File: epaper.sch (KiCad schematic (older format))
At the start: 34 parts, among them Q1 Q_NMOS_GSD, U1 SC18IS602B, U2 e-paper

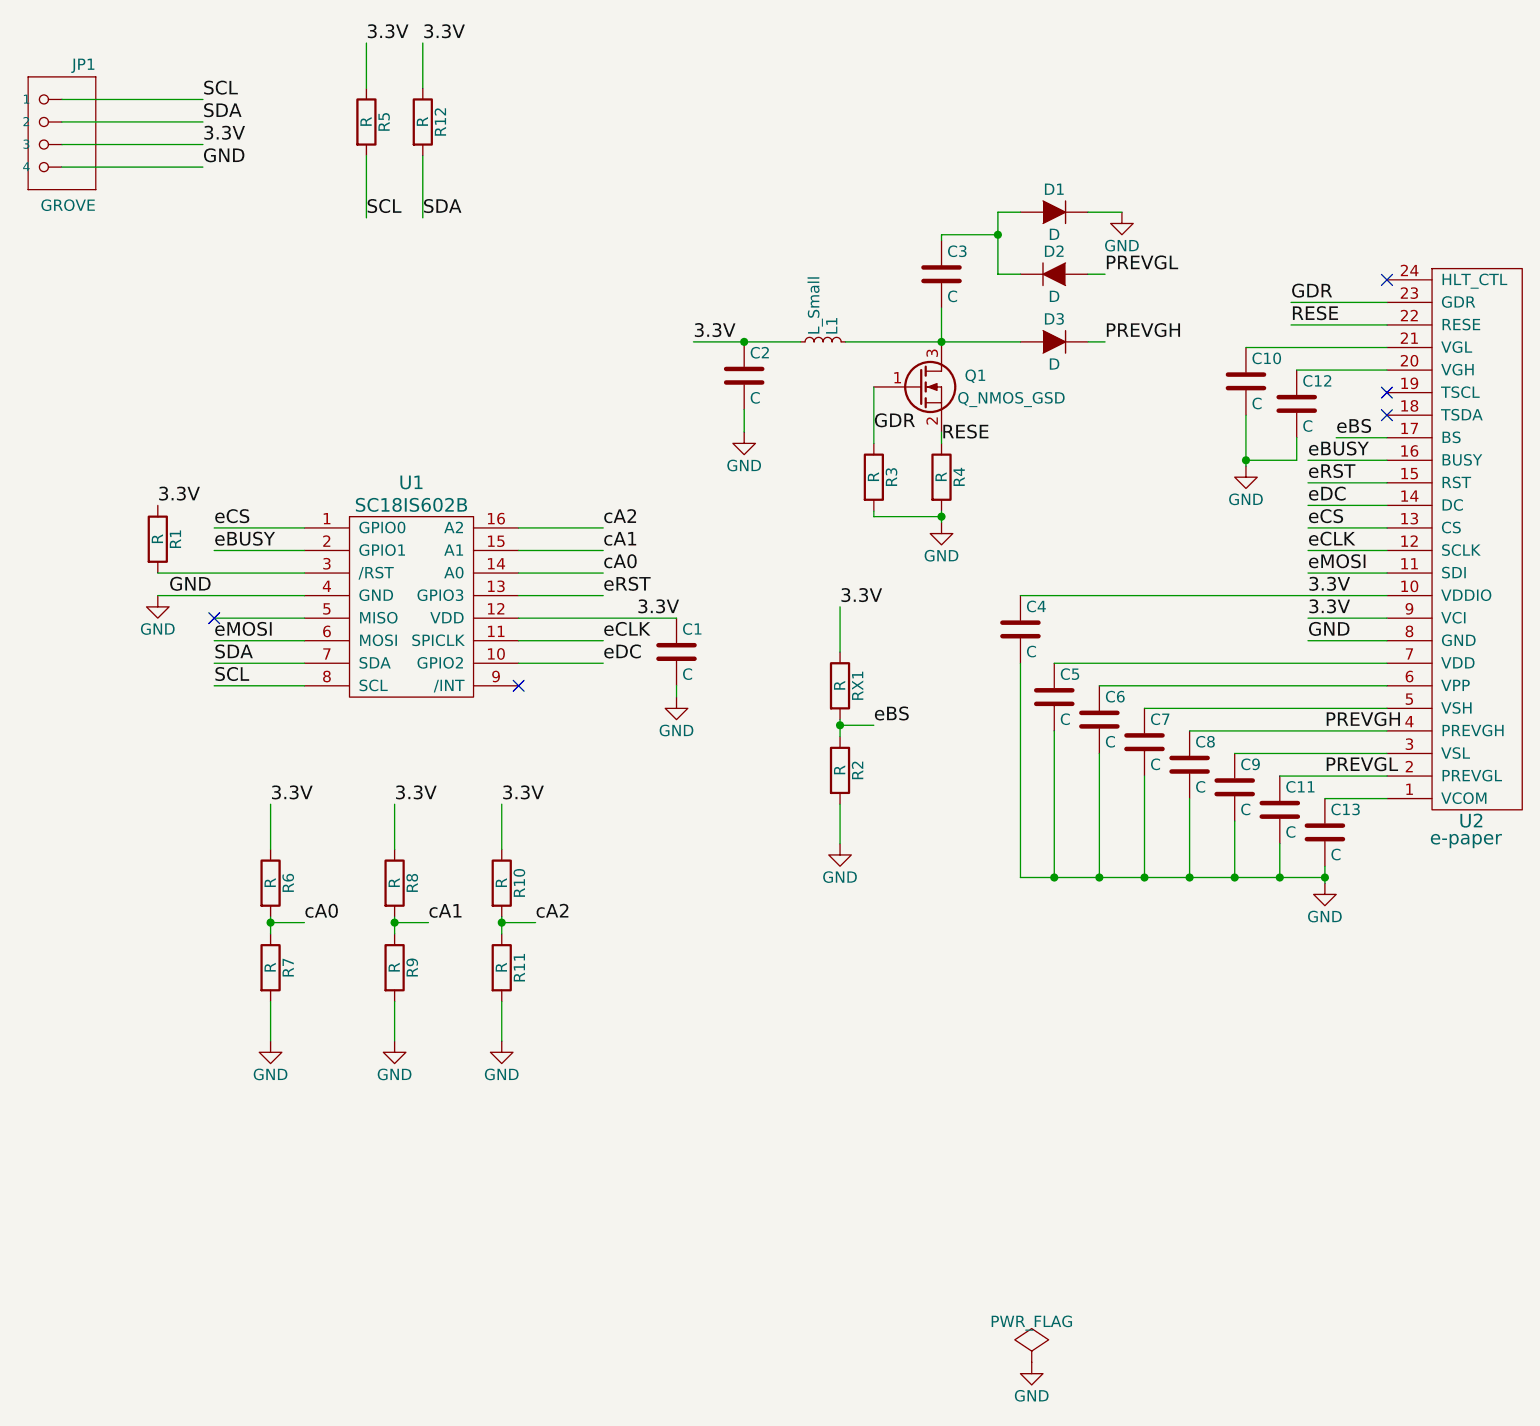
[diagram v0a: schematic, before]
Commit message: Fix the position of the HFL Connector
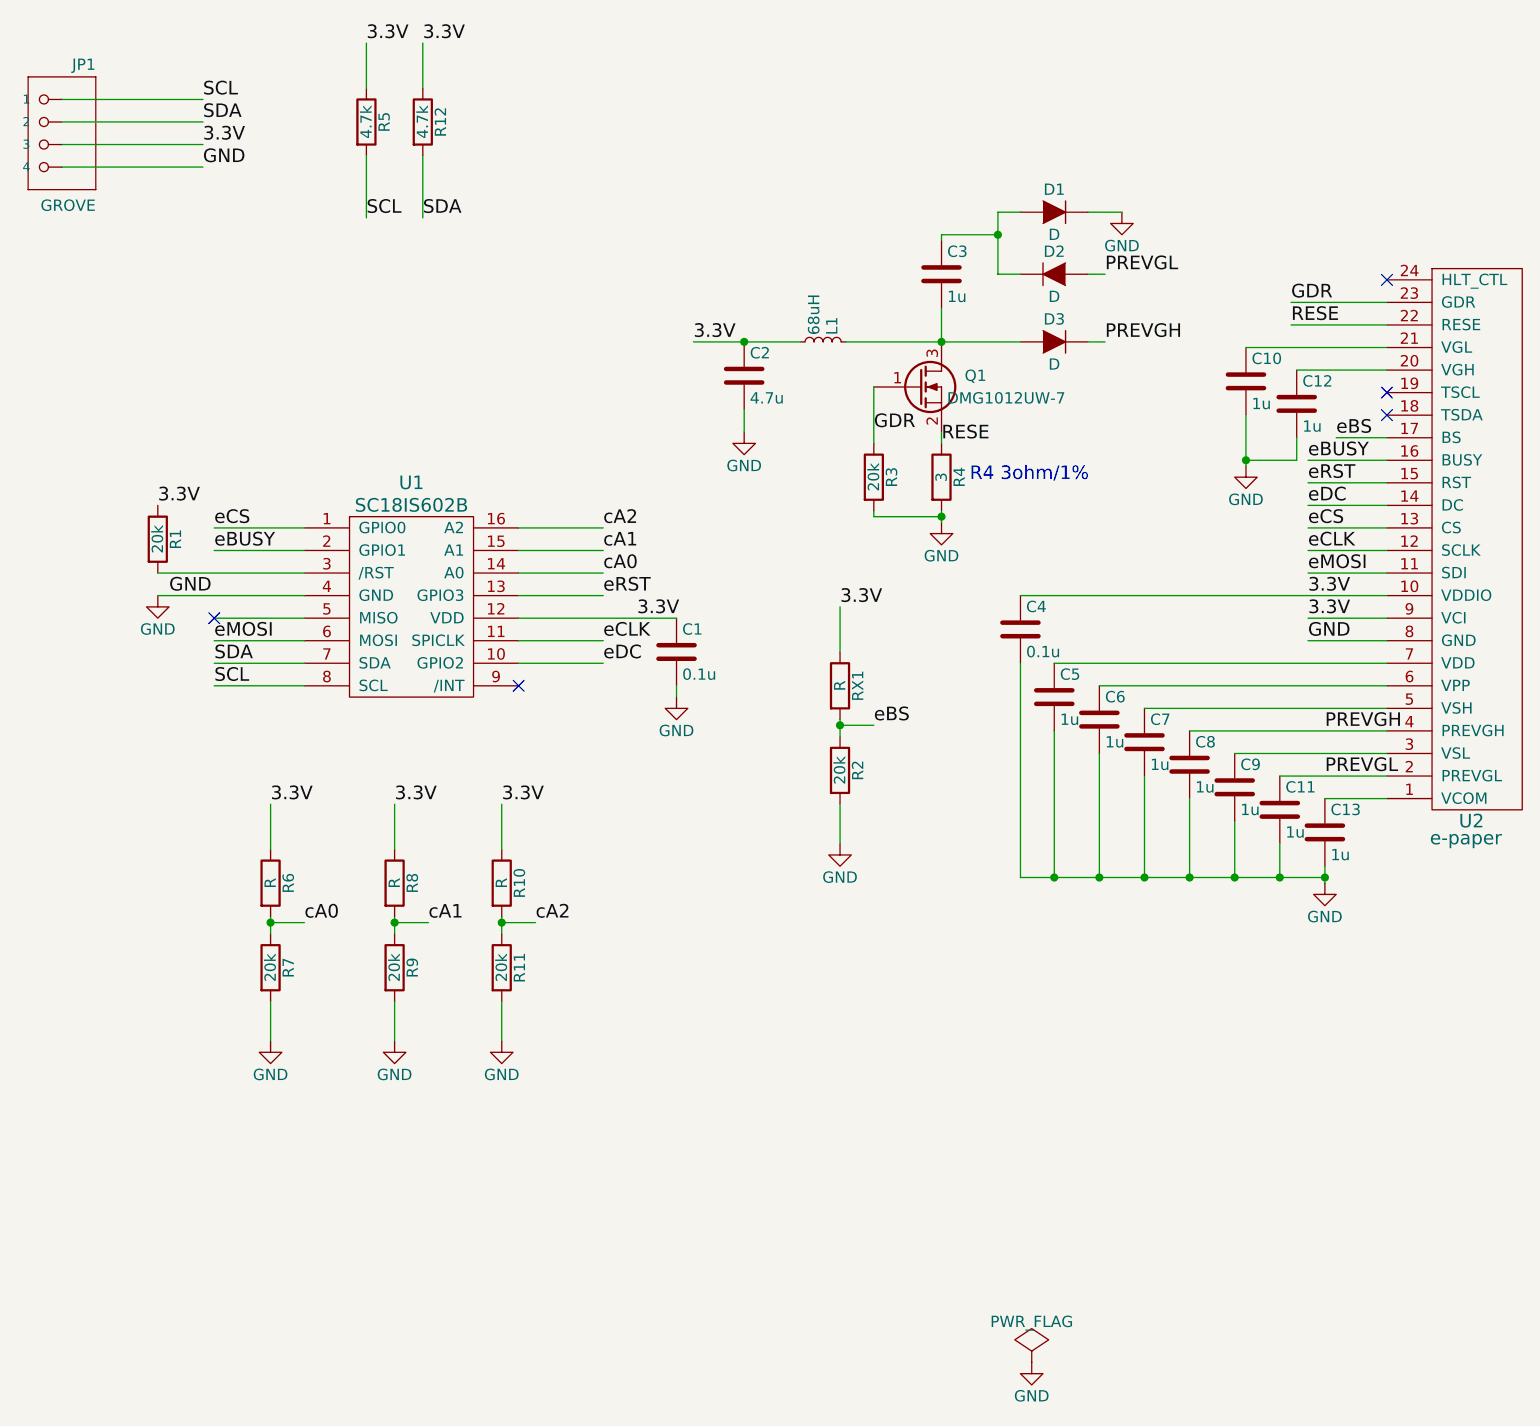
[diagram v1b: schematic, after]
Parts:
- C1, C4: value C -> 0.1u
- C10, C12, C13, C3, C5, C6, C7, C8, C9: value C -> 1u
- C11: value C -> 1u; Fieldname (none) -> Value
- C2: value C -> 4.7u
- L1: value L_Small -> 68uH
- Q1: value Q_NMOS_GSD -> DMG1012UW-7
- R1, R11, R2, R3, R9: value R -> 20k
- R12, R5: value R -> 4.7k
- R4: value R -> 3
- R7: value R -> 20k; Fieldname (none) -> Value
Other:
- note added: "R4 3ohm/1%"
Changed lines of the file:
@@
 encoding utf-8
 Sheet 1 1
-Title "e-Paper I2C Module"
+Title "e-Paper Grove Module"
 Date "2018-03-24"
 Rev "v1.0"
@@
 P 7800 4950
 F 0 "C13" H 7825 5050 50  0000 L CNN
-F 1 "C" H 7825 4850 50  0000 L CNN
+F 1 "1u" H 7825 4850 50  0000 L CNN
 F 2 "smt:C-0603" H 7838 4800 50  0001 C CNN
 F 3 "" H 7800 4950 50  0000 C CNN
@@
 P 7600 4850
 F 0 "C11" H 7625 4950 50  0000 L CNN
-F 1 "C" H 7625 4750 50  0000 L CNN
+F 1 "1u" H 7625 4750 50  0000 L CNN
 F 2 "smt:C-0603" H 7638 4700 50  0001 C CNN
 F 3 "" H 7600 4850 50  0000 C CNN
+F 4 "Value" H 7600 4850 60  0001 C CNN "Fieldname"
 	1    7600 4850
 	1    0    0    -1
@@
 P 7400 4750
 F 0 "C9" H 7425 4850 50  0000 L CNN
-F 1 "C" H 7425 4650 50  0000 L CNN
+F 1 "1u" H 7425 4650 50  0000 L CNN
 F 2 "smt:C-0603" H 7438 4600 50  0001 C CNN
 F 3 "" H 7400 4750 50  0000 C CNN
@@
 P 7200 4650
 F 0 "C8" H 7225 4750 50  0000 L CNN
-F 1 "C" H 7225 4550 50  0000 L CNN
+F 1 "1u" H 7225 4550 50  0000 L CNN
 F 2 "smt:C-0603" H 7238 4500 50  0001 C CNN
 F 3 "" H 7200 4650 50  0000 C CNN
@@
 $EndComp
 $Comp
-L GND #PWR12
+L GND #PWR01
 U 1 1 5AB51FE5
 P 7800 5175
-F 0 "#PWR12" H 7800 4925 50  0001 C CNN
+F 0 "#PWR01" H 7800 4925 50  0001 C CNN
 F 1 "GND" H 7800 5025 50  0000 C CNN
 F 2 "" H 7800 5175 50  0000 C CNN
@@
 P 7000 4550
 F 0 "C7" H 7025 4650 50  0000 L CNN
-F 1 "C" H 7025 4450 50  0000 L CNN
+F 1 "1u" H 7025 4450 50  0000 L CNN
 F 2 "smt:C-0603" H 7038 4400 50  0001 C CNN
 F 3 "" H 7000 4550 50  0000 C CNN
@@
 P 6800 4450
 F 0 "C6" H 6825 4550 50  0000 L CNN
-F 1 "C" H 6825 4350 50  0000 L CNN
+F 1 "1u" H 6825 4350 50  0000 L CNN
 F 2 "smt:C-0603" H 6838 4300 50  0001 C CNN
 F 3 "" H 6800 4450 50  0000 C CNN
@@
 P 6600 4350
 F 0 "C5" H 6625 4450 50  0000 L CNN
-F 1 "C" H 6625 4250 50  0000 L CNN
+F 1 "1u" H 6625 4250 50  0000 L CNN
 F 2 "smt:C-0603" H 6638 4200 50  0001 C CNN
 F 3 "" H 6600 4350 50  0000 C CNN
@@
 P 6450 4050
 F 0 "C4" H 6475 4150 50  0000 L CNN
-F 1 "C" H 6475 3950 50  0000 L CNN
+F 1 "0.1u" H 6475 3950 50  0000 L CNN
 F 2 "smt:C-0603" H 6488 3900 50  0001 C CNN
 F 3 "" H 6450 4050 50  0000 C CNN
@@
 P 7675 3050
 F 0 "C12" H 7700 3150 50  0000 L CNN
-F 1 "C" H 7700 2950 50  0000 L CNN
+F 1 "1u" H 7700 2950 50  0000 L CNN
 F 2 "smt:C-0603" H 7713 2900 50  0001 C CNN
 F 3 "" H 7675 3050 50  0000 C CNN
@@
 P 7450 2950
 F 0 "C10" H 7475 3050 50  0000 L CNN
-F 1 "C" H 7475 2850 50  0000 L CNN
+F 1 "1u" H 7475 2850 50  0000 L CNN
 F 2 "smt:C-0603" H 7488 2800 50  0001 C CNN
 F 3 "" H 7450 2950 50  0000 C CNN
@@
 $EndComp
 $Comp
-L GND #PWR11
+L GND #PWR02
 U 1 1 5AB52D16
 P 7450 3325
-F 0 "#PWR11" H 7450 3075 50  0001 C CNN
+F 0 "#PWR02" H 7450 3075 50  0001 C CNN
 F 1 "GND" H 7450 3175 50  0000 C CNN
 F 2 "" H 7450 3325 50  0000 C CNN
@@
 P 5575 2775
 F 0 "L1" H 5605 2815 50  0000 L CNN
-F 1 "L_Small" H 5605 2735 50  0000 L CNN
+F 1 "68uH" H 5605 2735 50  0000 L CNN
 F 2 "rcl:rcl-L3230M" H 5575 2775 50  0001 C CNN
 F 3 "" H 5575 2775 50  0000 C CNN
@@
 P 6000 2975
 F 0 "Q1" H 6300 3025 50  0000 R CNN
-F 1 "Q_NMOS_GSD" H 6650 2925 50  0000 R CNN
+F 1 "DMG1012UW-7" H 6650 2925 50  0000 R CNN
 F 2 "smt-sot:SOT23" H 6200 3075 50  0001 C CNN
 F 3 "" H 6000 2975 50  0000 C CNN
@@
 P 5650 4675
 F 0 "R2" V 5730 4675 50  0000 C CNN
-F 1 "R" V 5650 4675 50  0000 C CNN
+F 1 "20k" V 5650 4675 50  0000 C CNN
 F 2 "smt:R-0603" V 5580 4675 50  0001 C CNN
 F 3 "" H 5650 4675 50  0000 C CNN
@@
 $EndComp
 $Comp
-L GND #PWR7
+L GND #PWR03
 U 1 1 5AB560C2
 P 5650 5000
-F 0 "#PWR7" H 5650 4750 50  0001 C CNN
+F 0 "#PWR03" H 5650 4750 50  0001 C CNN
 F 1 "GND" H 5650 4850 50  0000 C CNN
 F 2 "" H 5650 5000 50  0000 C CNN
@@
 $EndComp
 $Comp
-L GND #PWR10
+L GND #PWR04
 U 1 1 5AB56C8D
 P 6900 2200
-F 0 "#PWR10" H 6900 1950 50  0001 C CNN
+F 0 "#PWR04" H 6900 1950 50  0001 C CNN
 F 1 "GND" H 6900 2050 50  0000 C CNN
 F 2 "" H 6900 2200 50  0000 C CNN
@@
 P 6100 2475
 F 0 "C3" H 6125 2575 50  0000 L CNN
-F 1 "C" H 6125 2375 50  0000 L CNN
+F 1 "1u" H 6125 2375 50  0000 L CNN
 F 2 "smt:C-0603" H 6138 2325 50  0001 C CNN
 F 3 "" H 6100 2475 50  0000 C CNN
@@
 P 6100 3375
 F 0 "R4" V 6180 3375 50  0000 C CNN
-F 1 "R" V 6100 3375 50  0000 C CNN
+F 1 "3" V 6100 3375 50  0000 C CNN
 F 2 "smt:R-0603" V 6030 3375 50  0001 C CNN
 F 3 "" H 6100 3375 50  0000 C CNN
@@
 P 5800 3375
 F 0 "R3" V 5880 3375 50  0000 C CNN
-F 1 "R" V 5800 3375 50  0000 C CNN
+F 1 "20k" V 5800 3375 50  0000 C CNN
 F 2 "smt:R-0603" V 5730 3375 50  0001 C CNN
 F 3 "" H 5800 3375 50  0000 C CNN
@@
 $EndComp
 $Comp
-L GND #PWR8
+L GND #PWR05
 U 1 1 5AB5837B
 P 6100 3575
-F 0 "#PWR8" H 6100 3325 50  0001 C CNN
+F 0 "#PWR05" H 6100 3325 50  0001 C CNN
 F 1 "GND" H 6100 3425 50  0000 C CNN
 F 2 "" H 6100 3575 50  0000 C CNN
@@
 P 5225 2925
 F 0 "C2" H 5250 3025 50  0000 L CNN
-F 1 "C" H 5250 2825 50  0000 L CNN
+F 1 "4.7u" H 5250 2825 50  0000 L CNN
 F 2 "smt:C-0603" H 5263 2775 50  0001 C CNN
 F 3 "" H 5225 2925 50  0000 C CNN
@@
 $EndComp
 $Comp
-L GND #PWR6
+L GND #PWR06
 U 1 1 5AB59D87
 P 5225 3175
-F 0 "#PWR6" H 5225 2925 50  0001 C CNN
+F 0 "#PWR06" H 5225 2925 50  0001 C CNN
 F 1 "GND" H 5225 3025 50  0000 C CNN
 F 2 "" H 5225 3175 50  0000 C CNN
@@
 	2625 3900 3275 3900
 $Comp
-L GND #PWR1
+L GND #PWR07
 U 1 1 5AB5C245
 P 2625 3900
-F 0 "#PWR1" H 2625 3650 50  0001 C CNN
+F 0 "#PWR07" H 2625 3650 50  0001 C CNN
 F 1 "GND" H 2625 3750 50  0000 C CNN
 F 2 "" H 2625 3900 50  0000 C CNN
@@
 P 4925 4150
 F 0 "C1" H 4950 4250 50  0000 L CNN
-F 1 "C" H 4950 4050 50  0000 L CNN
+F 1 "0.1u" H 4950 4050 50  0000 L CNN
 F 2 "smt:C-0603" H 4963 4000 50  0001 C CNN
 F 3 "" H 4925 4150 50  0000 C CNN
@@
 $EndComp
 $Comp
-L GND #PWR5
+L GND #PWR08
 U 1 1 5AB5C935
 P 4925 4350
-F 0 "#PWR5" H 4925 4100 50  0001 C CNN
+F 0 "#PWR08" H 4925 4100 50  0001 C CNN
 F 1 "GND" H 4925 4200 50  0000 C CNN
 F 2 "" H 4925 4350 50  0000 C CNN
@@
 P 2625 3650
 F 0 "R1" V 2705 3650 50  0000 C CNN
-F 1 "R" V 2625 3650 50  0000 C CNN
+F 1 "20k" V 2625 3650 50  0000 C CNN
 F 2 "smt:R-0603" V 2555 3650 50  0001 C CNN
 F 3 "" H 2625 3650 50  0000 C CNN
@@
 P 3125 5550
 F 0 "R7" V 3205 5550 50  0000 C CNN
-F 1 "R" V 3125 5550 50  0000 C CNN
+F 1 "20k" V 3125 5550 50  0000 C CNN
 F 2 "smt:R-0603" V 3055 5550 50  0001 C CNN
 F 3 "" H 3125 5550 50  0000 C CNN
+F 4 "Value" H 3125 5550 60  0001 C CNN "Fieldname"
 	1    3125 5550
 	1    0    0    -1
 $EndComp
 $Comp
-L GND #PWR2
+L GND #PWR09
 U 1 1 5AB600EF
 P 3125 5875
-F 0 "#PWR2" H 3125 5625 50  0001 C CNN
+F 0 "#PWR09" H 3125 5625 50  0001 C CNN
 F 1 "GND" H 3125 5725 50  0000 C CNN
 F 2 "" H 3125 5875 50  0000 C CNN
@@
 P 3675 5550
 F 0 "R9" V 3755 5550 50  0000 C CNN
-F 1 "R" V 3675 5550 50  0000 C CNN
+F 1 "20k" V 3675 5550 50  0000 C CNN
 F 2 "smt:R-0603" V 3605 5550 50  0001 C CNN
 F 3 "" H 3675 5550 50  0000 C CNN
@@
 $EndComp
 $Comp
-L GND #PWR3
+L GND #PWR010
 U 1 1 5AB601D8
 P 3675 5875
-F 0 "#PWR3" H 3675 5625 50  0001 C CNN
+F 0 "#PWR010" H 3675 5625 50  0001 C CNN
 F 1 "GND" H 3675 5725 50  0000 C CNN
 F 2 "" H 3675 5875 50  0000 C CNN
@@
 P 4150 5550
 F 0 "R11" V 4230 5550 50  0000 C CNN
-F 1 "R" V 4150 5550 50  0000 C CNN
+F 1 "20k" V 4150 5550 50  0000 C CNN
 F 2 "smt:R-0603" V 4080 5550 50  0001 C CNN
 F 3 "" H 4150 5550 50  0000 C CNN
@@
 $EndComp
 $Comp
-L GND #PWR4
+L GND #PWR011
 U 1 1 5AB60259
 P 4150 5875
-F 0 "#PWR4" H 4150 5625 50  0001 C CNN
+F 0 "#PWR011" H 4150 5625 50  0001 C CNN
 F 1 "GND" H 4150 5725 50  0000 C CNN
 F 2 "" H 4150 5875 50  0000 C CNN
@@
 cA2
 $Comp
-L GND #PWR9
+L GND #PWR012
 U 1 1 5AB61533
 P 6500 7300
-F 0 "#PWR9" H 6500 7050 50  0001 C CNN
+F 0 "#PWR012" H 6500 7050 50  0001 C CNN
 F 1 "GND" H 6500 7150 50  0000 C CNN
 F 2 "" H 6500 7300 50  0000 C CNN
@@
 $EndComp
 $Comp
-L PWR_FLAG #FLG1
+L PWR_FLAG #FLG013
 U 1 1 5AB61CE0
 P 6500 7300
-F 0 "#FLG1" H 6500 7395 50  0001 C CNN
+F 0 "#FLG013" H 6500 7395 50  0001 C CNN
 F 1 "PWR_FLAG" H 6500 7480 50  0000 C CNN
 F 2 "" H 6500 7300 50  0000 C CNN
@@
 P 3550 1800
 F 0 "R5" V 3630 1800 50  0000 C CNN
-F 1 "R" V 3550 1800 50  0000 C CNN
+F 1 "4.7k" V 3550 1800 50  0000 C CNN
 F 2 "smt:R-0603" V 3480 1800 50  0001 C CNN
 F 3 "" H 3550 1800 50  0000 C CNN
@@
 P 3800 1800
 F 0 "R12" V 3880 1800 50  0000 C CNN
-F 1 "R" V 3800 1800 50  0000 C CNN
+F 1 "4.7k" V 3800 1800 50  0000 C CNN
 F 2 "smt:R-0603" V 3730 1800 50  0001 C CNN
 F 3 "" H 3800 1800 50  0000 C CNN
@@
 Text Label 2675 3900 0    60   ~ 0
 GND
+Text Notes 6225 3400 0    60   ~ 0
+R4 3ohm/1%
 $EndSCHEMATC
